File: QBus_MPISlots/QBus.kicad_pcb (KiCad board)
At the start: 2 copper layers, 165 x 160 mm, 5 parts, among them J1 QBUSDUAL, J2 QBUSDUAL, J3 QBUSDUAL, J4 QBUSDUAL, J5 IDC-64M

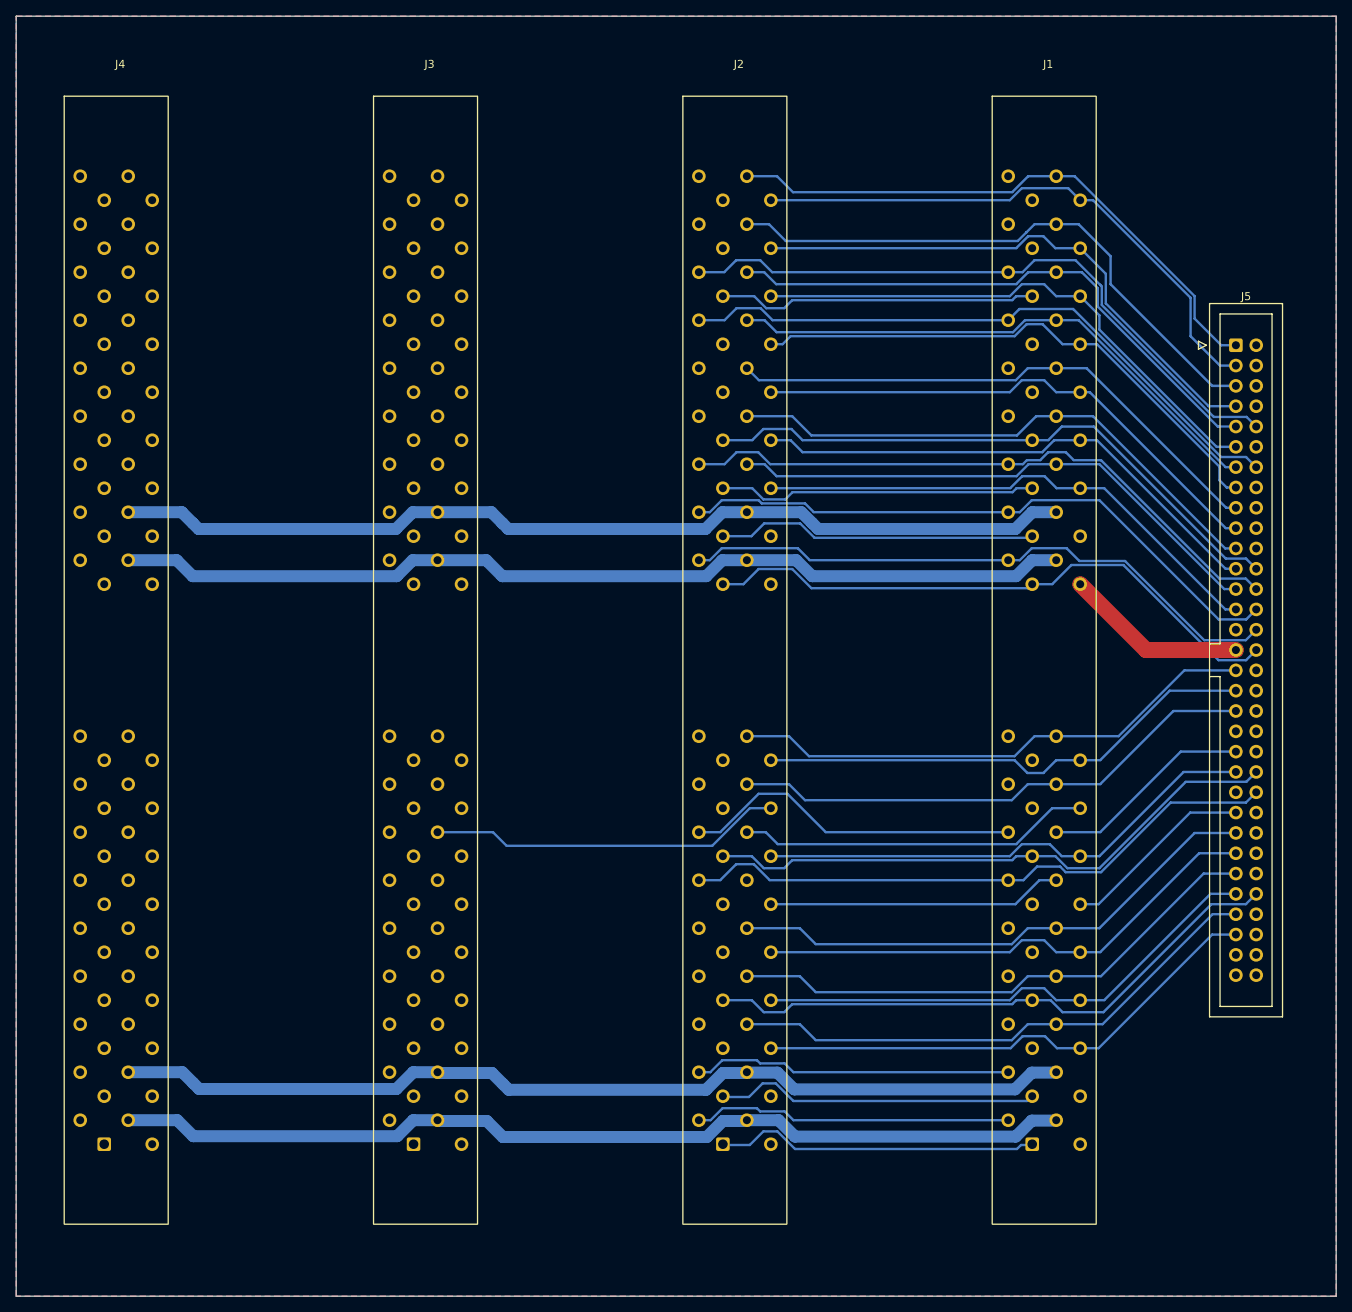
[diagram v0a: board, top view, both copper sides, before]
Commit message: QBus_MPISlots: Re-layout
Moved MPI connectors, too far apart and too close to case wall and main board.
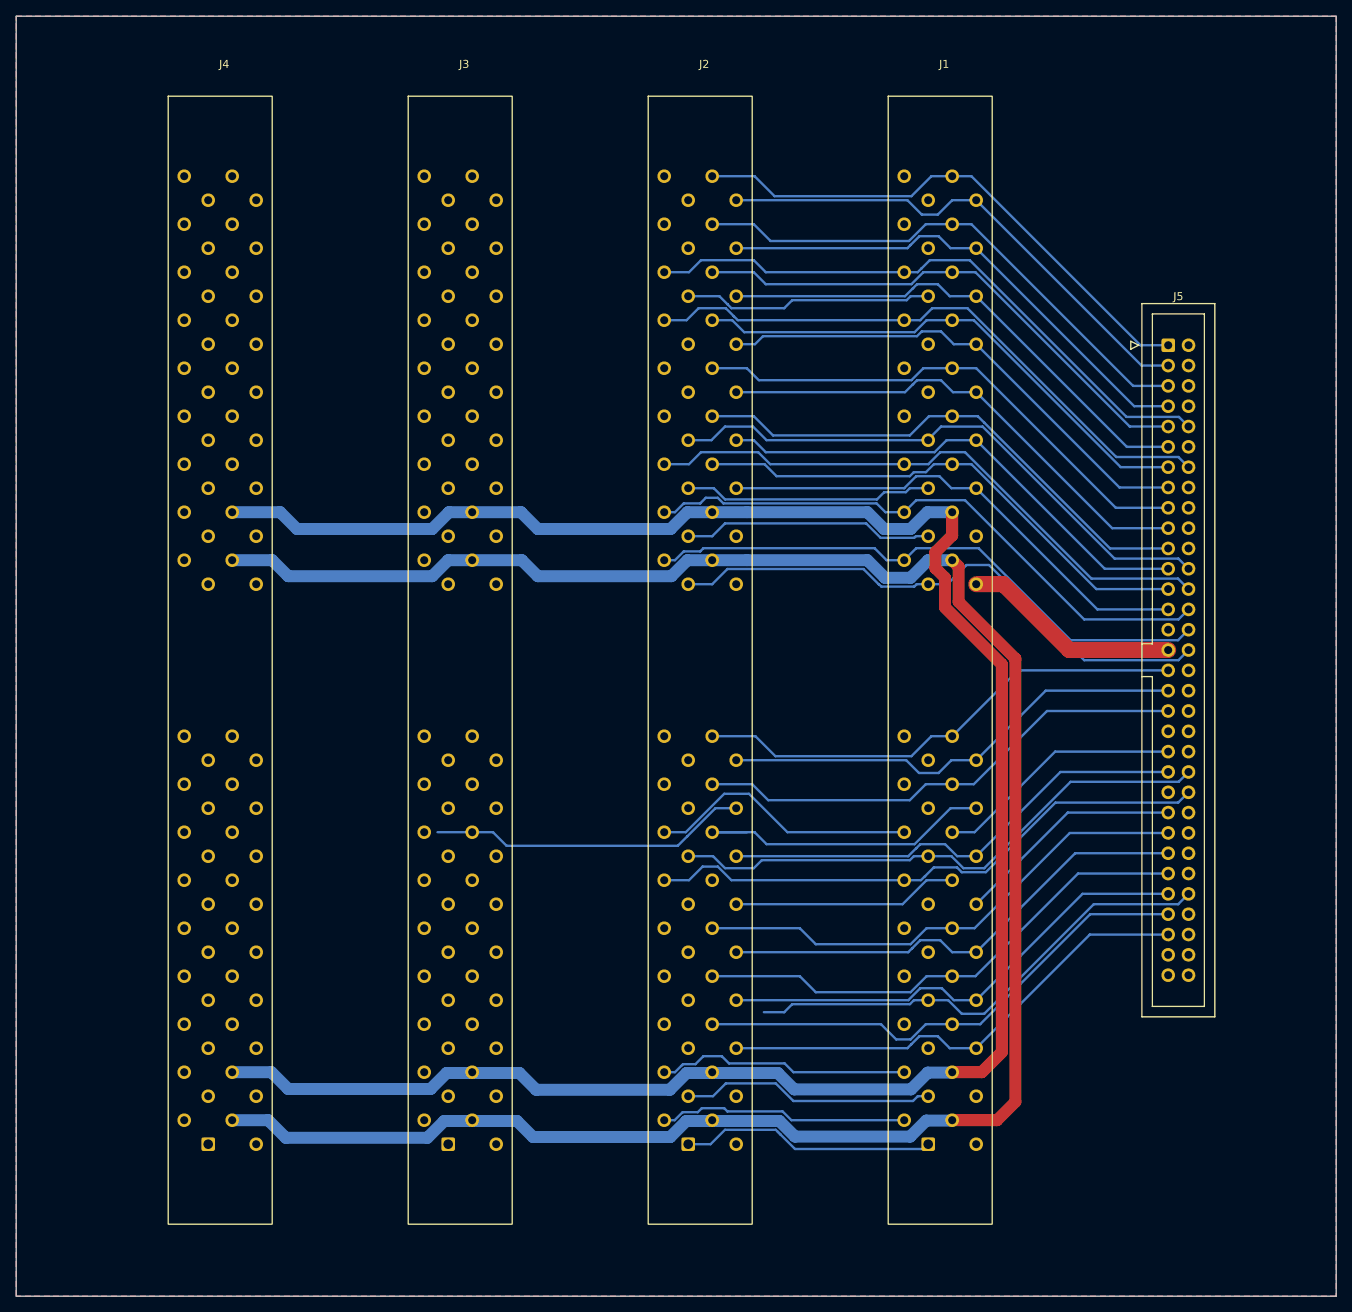
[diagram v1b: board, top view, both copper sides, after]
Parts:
- moved J4 13.0 mm to (42.3, 180.5)
- moved J1 13.0 mm to (132.3, 180.5)
- moved J5 8.46 mm to (164.8, 111.6)
- moved J2 4.33 mm to (102.3, 180.5)
- moved J3 4.33 mm to (72.3, 180.5)
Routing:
- net -12V: track 242.0 -> 270.0 mm
- net +12V: track 242.4 -> 269.4 mm
- net /~{I_HALT}: track 74.7 -> 60.6 mm
- net /SSpare4: track 40.2 -> 31.5 mm
- net Net-(J1-BIAKO): track 36.9 -> 28.2 mm
- net /~{BREF}: track 42.6 -> 34.0 mm
- net /SSpare6: track 39.8 -> 31.2 mm
- net /Pspare6: track 39.9 -> 31.2 mm
- net /Bspare2: track 39.9 -> 31.2 mm
- net /~{BDAL16}: track 40.4 -> 31.8 mm
- net /~{BDAL17}: track 39.9 -> 31.7 mm
- net /Bspare1: track 40.4 -> 32.4 mm
- net /~{BDAL14}: track 70.7 -> 64.1 mm
- net /~{BDAL12}: track 69.7 -> 63.4 mm
- net /~{BDAL13}: track 73.3 -> 67.1 mm
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
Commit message: QBus_MPISlots: Add 12V connectors
12V voltages aren't present on the main connector. Use auxiliary ATX connector
for +12V and extra pins for -12V.
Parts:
- added J6: Conn_02x02_Top_Bottom, Connector_Molex:Molex_Mini-Fit_Jr_5566-04A_2x02_P4.20mm_Vertical, F.Cu at (157.7, 202.6)
- added J7: Conn_01x03, Connector_Wago:Wago_734-133_1x03_P3.50mm_Vertical, F.Cu at (166.3, 202.5)
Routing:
- net -12V: track 270.0 -> 299.6 mm
- net +12V: track 269.4 -> 297.9 mm
- net /~{I_HALT}: track 60.6 -> 70.7 mm
- net Net-(J1-BDMGO): track 39.8 -> 35.5 mm
- net Net-(J2-BDMGO): track 40.0 -> 35.7 mm
